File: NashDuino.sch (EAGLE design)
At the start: 28 parts, among them IC1 MEGA8-AI, IC2 FT232RL, SW1 SKHMPSE010, U3 V_REG_MIC2920, Y1 CSTCR6M00G53Z

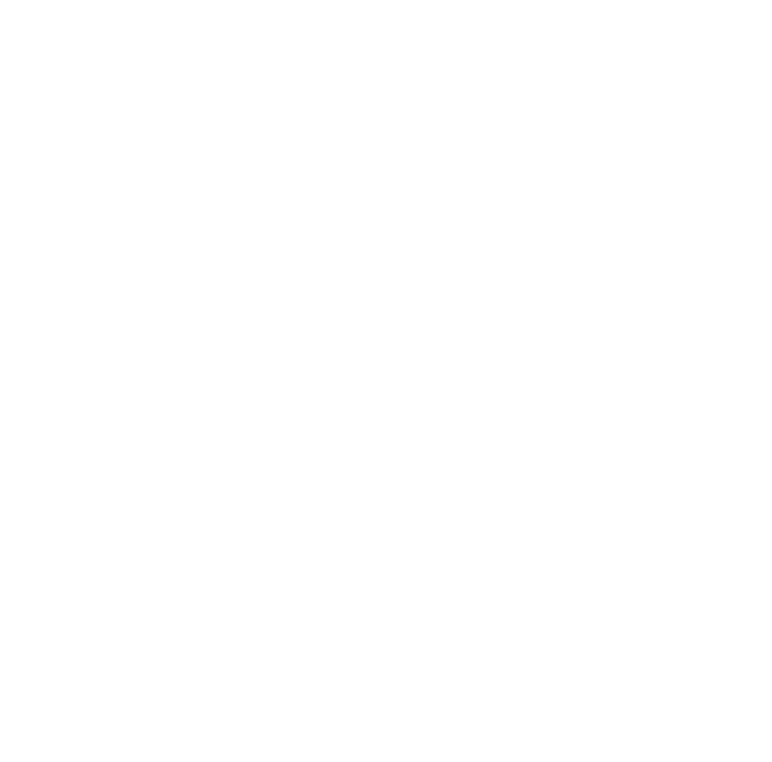
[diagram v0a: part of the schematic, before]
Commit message: Added Gadgeteer socket.
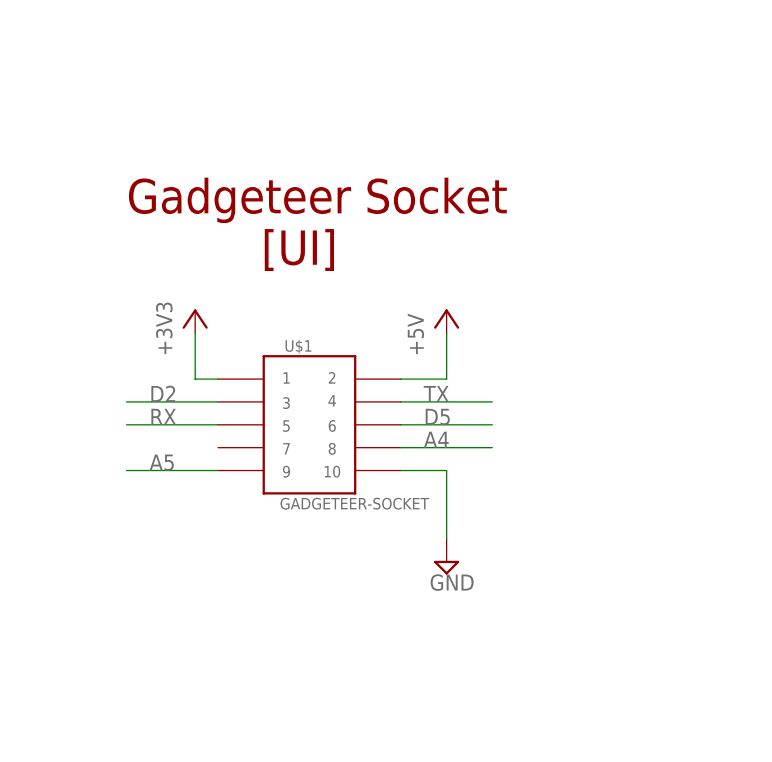
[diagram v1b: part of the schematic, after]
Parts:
- added U$1: GADGETEER-SOCKET, SoftDust:GADGETEER-SOCKET
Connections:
- net +3V3: now also U$1.P$1
- net +5V: now also U$1.P$2
- net A4: now also U$1.P$8
- net A5: now also U$1.P$9
- net D2: now also U$1.P$3
- net D5: now also U$1.P$6
- net GND: now also U$1.P$10
- net RX: now also U$1.P$5
- net TX: now also U$1.P$4
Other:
- note added: "Gadgeteer Socket [UI]"
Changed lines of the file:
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@@
 <layer number="106" name="bPlate" color="7" fill="1" visible="no" active="yes"/>
 <layer number="107" name="Crop" color="7" fill="1" visible="no" active="yes"/>
+<layer number="108" name="fp8" color="7" fill="1" visible="yes" active="yes"/>
+<layer number="109" name="fp9" color="7" fill="1" visible="yes" active="yes"/>
+<layer number="110" name="fp0" color="7" fill="1" visible="yes" active="yes"/>
 <layer number="116" name="Patch_BOT" color="9" fill="4" visible="no" active="yes"/>
 <layer number="121" name="_tsilk" color="7" fill="1" visible="no" active="yes"/>
 <layer number="122" name="_bsilk" color="7" fill="1" visible="no" active="yes"/>
+<layer number="123" name="tTestmark" color="7" fill="1" visible="yes" active="yes"/>
+<layer number="124" name="bTestmark" color="7" fill="1" visible="yes" active="yes"/>
 <layer number="125" name="_tNames" color="7" fill="1" visible="no" active="yes"/>
+<layer number="131" name="tAdjust" color="7" fill="1" visible="yes" active="yes"/>
+<layer number="132" name="bAdjust" color="7" fill="1" visible="yes" active="yes"/>
 <layer number="144" name="Drill_legend" color="7" fill="1" visible="no" active="yes"/>
 <layer number="151" name="HeatSink" color="7" fill="1" visible="no" active="yes"/>
@@
 <part name="C9" library="eagle-ltspice" deviceset="C" device="C1206" value="0.1uF"/>
 <part name="SUPPLY12" library="supply2" deviceset="GND" device=""/>
+<part name="U$1" library="SoftDust" deviceset="GADGETEER-SOCKET" device=""/>
+<part name="+3V3" library="supply1" deviceset="+3V3" device=""/>
+<part name="P+11" library="supply1" deviceset="+5V" device=""/>
+<part name="SUPPLY13" library="supply2" deviceset="GND" device=""/>
 </parts>
 <sheets>
@@
 <text x="167.64" y="175.26" size="3.81" layer="94">Arduino</text>
 <text x="317.5" y="175.26" size="3.81" layer="94">USB</text>
+<text x="20.32" y="154.94" size="3.81" layer="94">Gadgeteer Socket
+          [UI]</text>
 </plain>
 <instances>
@@
 </instance>
 <instance part="SUPPLY12" gate="GND" x="386.08" y="58.42"/>
+<instance part="U$1" gate="G$1" x="40.64" y="137.16"/>
+<instance part="+3V3" gate="G$1" x="27.94" y="149.86"/>
+<instance part="P+11" gate="1" x="55.88" y="149.86"/>
+<instance part="SUPPLY13" gate="GND" x="55.88" y="121.92"/>
 </instances>
 <busses>
@@
 <wire x1="378.46" y1="63.5" x2="386.08" y2="63.5" width="0.3048" layer="91"/>
 </segment>
+<segment>
+<pinref part="U$1" gate="G$1" pin="P$10"/>
+<pinref part="SUPPLY13" gate="GND" pin="GND"/>
+<wire x1="50.8" y1="132.08" x2="55.88" y2="132.08" width="0.1524" layer="91"/>
+<wire x1="55.88" y1="132.08" x2="55.88" y2="124.46" width="0.1524" layer="91"/>
+</segment>
 </net>
 <net name="N$5" class="0">
@@
 <label x="88.9" y="226.06" size="1.778" layer="95"/>
 </segment>
+<segment>
+<pinref part="U$1" gate="G$1" pin="P$8"/>
+<wire x1="50.8" y1="134.62" x2="60.96" y2="134.62" width="0.1524" layer="91"/>
+<label x="53.34" y="134.62" size="1.778" layer="95"/>
+</segment>
 </net>
 <net name="A5" class="0">
@@
 <wire x1="78.74" y1="228.6" x2="101.6" y2="228.6" width="0.3048" layer="91"/>
 <label x="88.9" y="228.6" size="1.778" layer="95"/>
+</segment>
+<segment>
+<pinref part="U$1" gate="G$1" pin="P$9"/>
+<wire x1="30.48" y1="132.08" x2="20.32" y2="132.08" width="0.1524" layer="91"/>
+<label x="22.86" y="132.08" size="1.778" layer="95"/>
 </segment>
 </net>
@@
 <label x="203.2" y="132.08" size="1.778" layer="95"/>
 </segment>
+<segment>
+<pinref part="U$1" gate="G$1" pin="P$3"/>
+<wire x1="30.48" y1="139.7" x2="20.32" y2="139.7" width="0.1524" layer="91"/>
+<label x="22.86" y="139.7" size="1.778" layer="95"/>
+</segment>
 </net>
 <net name="D3" class="0">
@@
 <wire x1="200.66" y1="124.46" x2="208.28" y2="124.46" width="0.3048" layer="91"/>
 <label x="203.2" y="124.46" size="1.778" layer="95"/>
+</segment>
+<segment>
+<pinref part="U$1" gate="G$1" pin="P$6"/>
+<wire x1="50.8" y1="137.16" x2="60.96" y2="137.16" width="0.1524" layer="91"/>
+<label x="53.34" y="137.16" size="1.778" layer="95"/>
 </segment>
 </net>
@@
 <wire x1="396.24" y1="165.1" x2="396.24" y2="175.26" width="0.3048" layer="91"/>
 </segment>
+<segment>
+<pinref part="U$1" gate="G$1" pin="P$2"/>
+<pinref part="P+11" gate="1" pin="+5V"/>
+<wire x1="50.8" y1="142.24" x2="55.88" y2="142.24" width="0.1524" layer="91"/>
+<wire x1="55.88" y1="142.24" x2="55.88" y2="147.32" width="0.1524" layer="91"/>
+</segment>
 </net>
 <net name="+3V3" class="0">
@@
 <junction x="271.78" y="129.54"/>
 </segment>
+<segment>
+<pinref part="U$1" gate="G$1" pin="P$1"/>
+<pinref part="+3V3" gate="G$1" pin="+3V3"/>
+<wire x1="30.48" y1="142.24" x2="27.94" y2="142.24" width="0.1524" layer="91"/>
+<wire x1="27.94" y1="142.24" x2="27.94" y2="147.32" width="0.1524" layer="91"/>
+</segment>
 </net>
 <net name="TX" class="0">
@@
 <wire x1="337.82" y1="154.94" x2="350.52" y2="154.94" width="0.3048" layer="91"/>
 <label x="340.36" y="154.94" size="1.778" layer="95"/>
+</segment>
+<segment>
+<pinref part="U$1" gate="G$1" pin="P$4"/>
+<wire x1="50.8" y1="139.7" x2="60.96" y2="139.7" width="0.1524" layer="91"/>
+<label x="53.34" y="139.7" size="1.778" layer="95"/>
 </segment>
 </net>
@@
 <label x="228.6" y="137.16" size="1.778" layer="95"/>
 </segment>
+<segment>
+<pinref part="U$1" gate="G$1" pin="P$5"/>
+<wire x1="30.48" y1="137.16" x2="20.32" y2="137.16" width="0.1524" layer="91"/>
+<label x="22.86" y="137.16" size="1.778" layer="95"/>
+</segment>
 </net>
 <net name="N$7" class="0">
@@
 </schematic>
 </drawing>
+<compatibility>
+<note version="6.3" minversion="6.2.2" severity="warning">
+Since Version 6.2.2 text objects can contain more than one line,
+which will not be processed correctly with this version.
+</note>
+</compatibility>
 </eagle>
